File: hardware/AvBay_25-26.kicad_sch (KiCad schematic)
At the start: 16 parts, among them SW1 SW_SPST, SW2 SW_SPST, SW3 SW_SPST

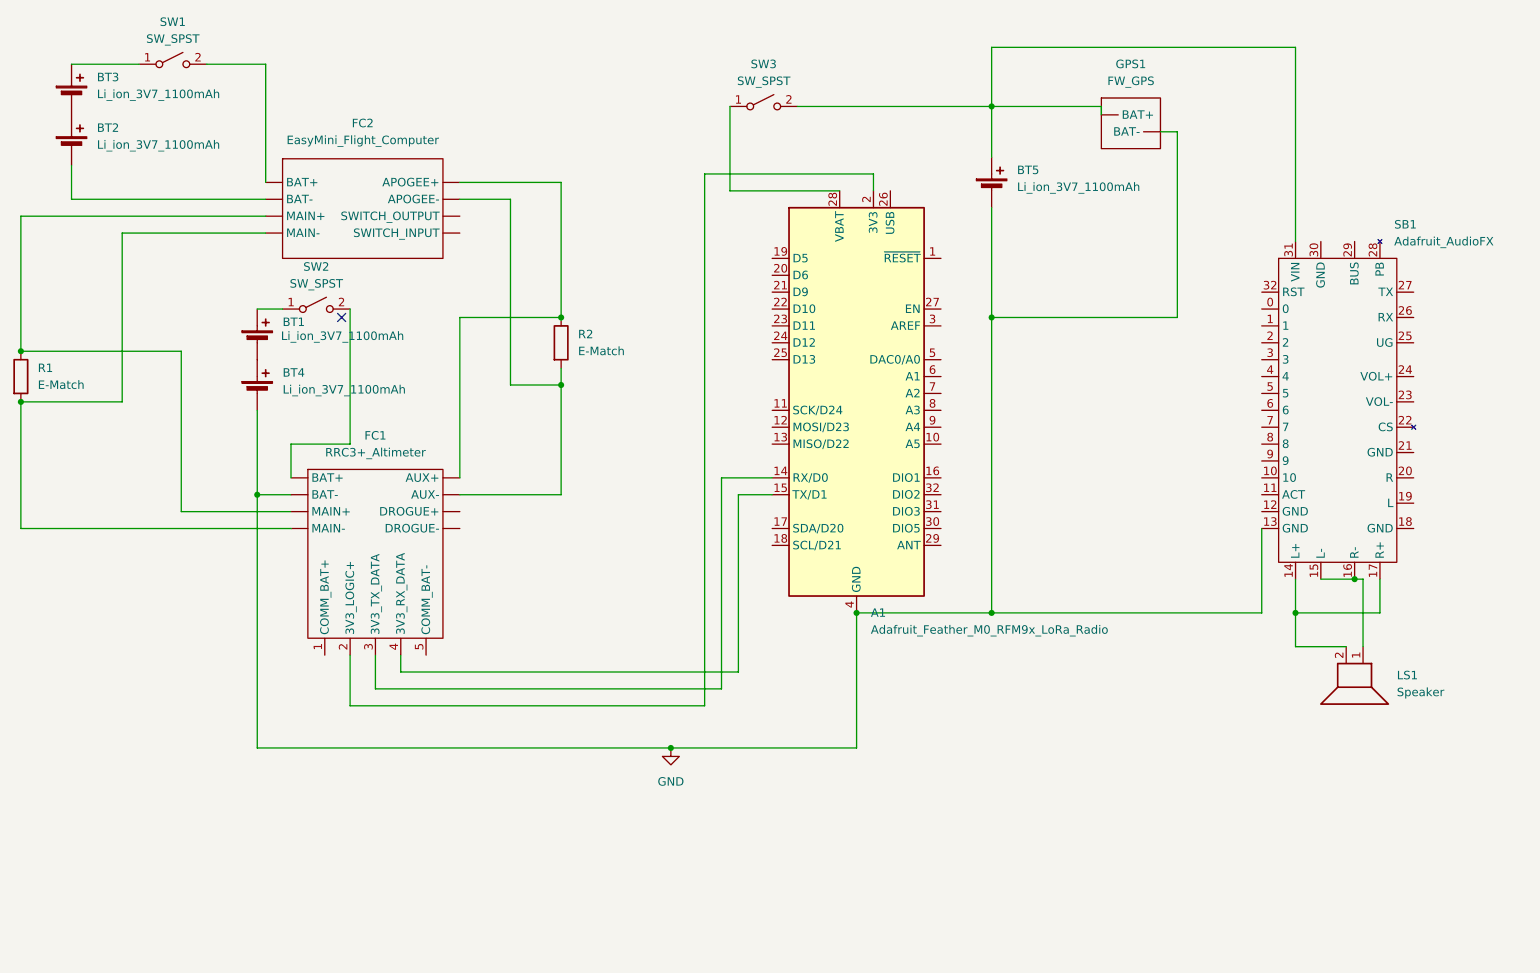
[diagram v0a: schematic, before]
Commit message: feat: add live video
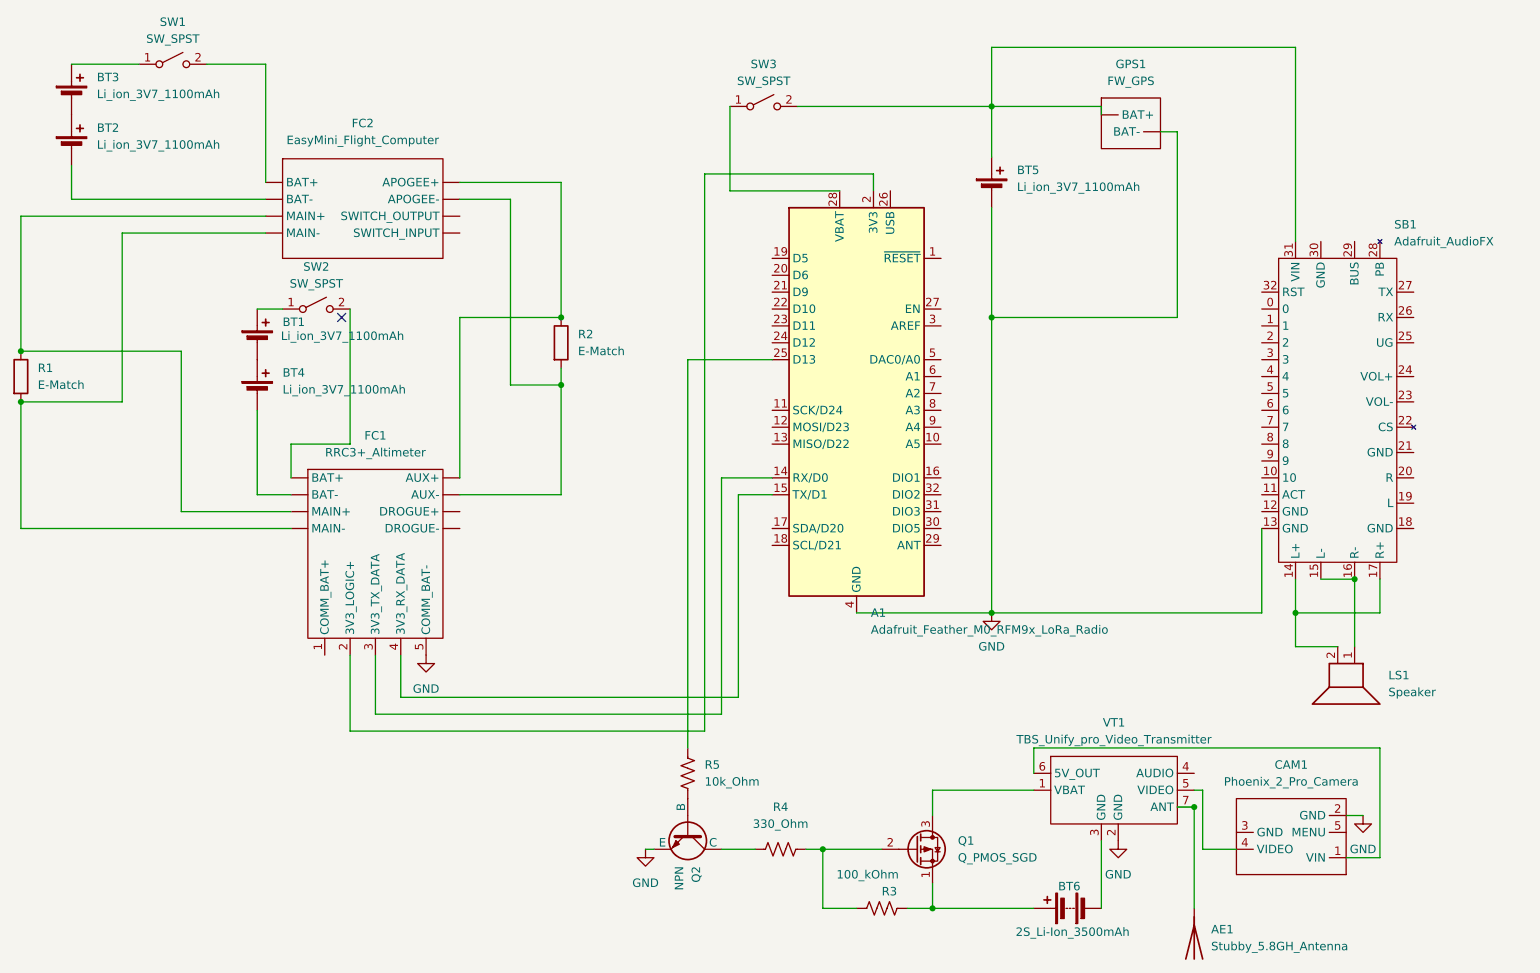
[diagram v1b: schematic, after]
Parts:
- added AE1: Stubby_5.8GH_Antenna, symbol Device:Antenna
- added BT6: 2S_Li-Ion_3500mAh, symbol Device:Battery
- added CAM1: Phoenix_2_Pro_Camera, symbol Avionics_Devices:Runcam_Phoenix_Pro_2
- added Q1: Q_PMOS_SGD, symbol Transistor_FET:Q_PMOS_SGD
- added Q2: NPN, symbol Simulation_SPICE:NPN
- added R3: 100_kOhm, symbol Device:R_US
- added R4: 330_Ohm, symbol Device:R_US
- added R5: 10k_Ohm, symbol Device:R_US
- added VT1: TBS_Unify_pro_Video_Transmitter, symbol Avionics_Devices:TBS_Unify_Pro_5G8_HV_25-800mW_Video_Transmitter_(SMA)
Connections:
- net GND: now also FC1.5 (COMM_BAT-), CAM1.2 (GND), Q2.3 (E), VT1.2 (GND); no longer BT4.2 (-), FC1. (DROGUE-)
- net at FC1. (DROGUE-): now also SW2.2 (B)
- net at FC2. (SWITCH_INPUT): now also BT2.2 (-)
- net at A1.25 (D13): now also R5.1
- new net: BT4.2 (-), FC1. (DROGUE-)
- new net: Q1.3 (D), VT1.1 (VBAT)
- new net: BT6.2 (-), VT1.3 (GND)
- new net: CAM1.4 (VIDEO), VT1.5 (VIDEO)
- new net: CAM1.1 (VIN), VT1.6 (5V_OUT)
- new net: AE1.1 (A), VT1.7 (ANT)
- new net: FC1. (DROGUE-), FC2. (SWITCH_INPUT), R1.1
- new net: FC1. (DROGUE-), FC2. (SWITCH_INPUT), R1.2
- new net: FC1. (DROGUE-), FC2. (SWITCH_INPUT), R2.1
- new net: FC1. (DROGUE-), FC2. (SWITCH_INPUT), R2.2
- new net: Q2.1 (C), R4.1
- new net: Q1.2 (G), R3.1, R4.2
- new net: Q2.2 (B), R5.2
- new net: BT6.1 (+), Q1.1 (S), R3.2
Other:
- moved on the sheet: LS1

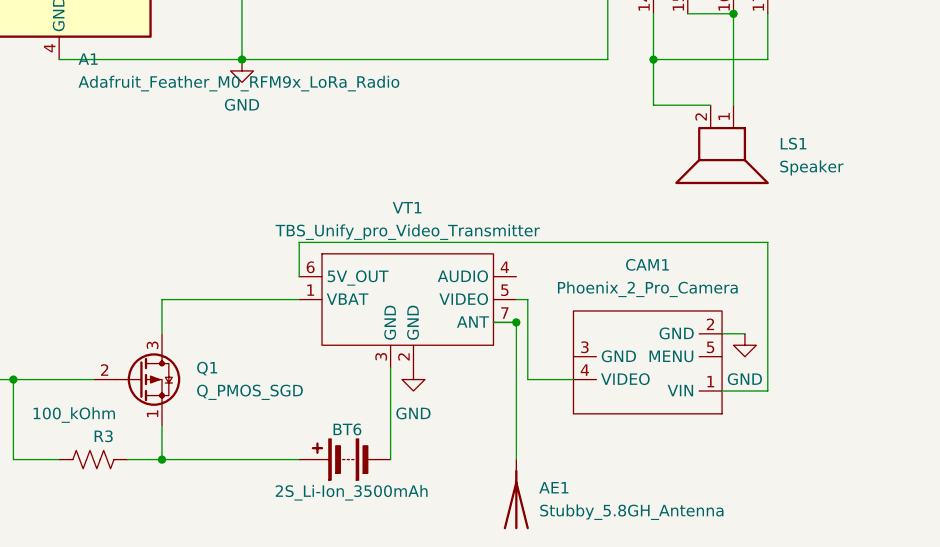
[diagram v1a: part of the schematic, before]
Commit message: feat: onboard video
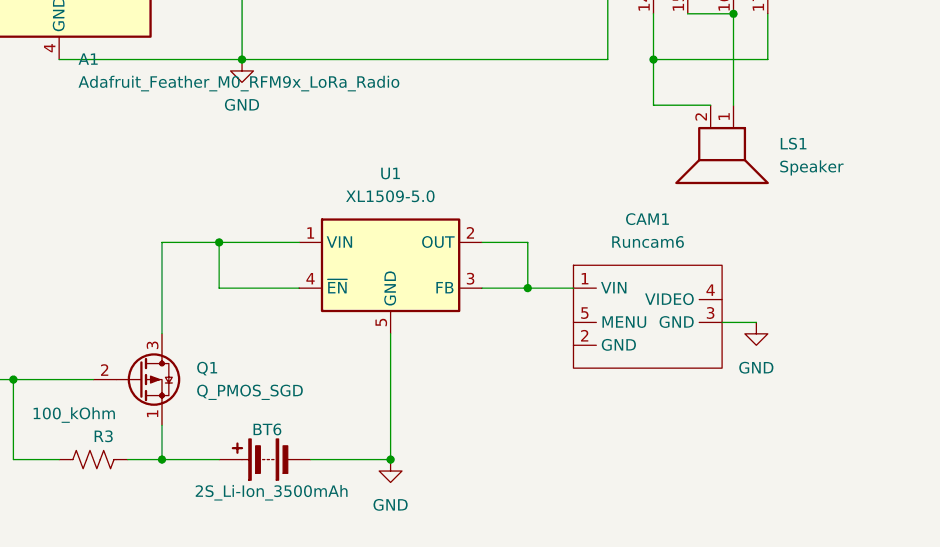
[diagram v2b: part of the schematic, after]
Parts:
- removed AE1: Stubby_5.8GH_Antenna, symbol Device:Antenna
- removed VT1: TBS_Unify_pro_Video_Transmitter, symbol Avionics_Devices:TBS_Unify_Pro_5G8_HV_25-800mW_Video_Transmitter_(SMA)
- added U1: XL1509-5.0, Package_SO:SOIC-8_3.9x4.9mm_P1.27mm, symbol Regulator_Switching:XL1509-5.0
- CAM1: value Phoenix_2_Pro_Camera -> Runcam6
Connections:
- net GND: now also BT6.2 (-), CAM1.3 (GND), U1.5 (GND), U1.6 (GND), U1.7 (GND), U1.8 (GND); no longer CAM1.2 (GND)
- net at Q1.3 (D): now also U1.1 (VIN), U1.4 (~{EN})
- net at CAM1.1 (VIN): now also U1.2 (OUT), U1.3 (FB)
- net at FC1. (DROGUE-): now also SW2.2 (B)
- net at FC2. (SWITCH_INPUT): now also BT2.2 (-)
- new net: FC1. (DROGUE-), FC2. (SWITCH_INPUT), R1.1
- new net: FC1. (DROGUE-), FC2. (SWITCH_INPUT), R1.2
- new net: FC1. (DROGUE-), FC2. (SWITCH_INPUT), R2.1
- new net: FC1. (DROGUE-), FC2. (SWITCH_INPUT), R2.2
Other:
- moved on the sheet: BT6, CAM1
